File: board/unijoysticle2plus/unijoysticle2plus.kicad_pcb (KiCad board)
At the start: 2 copper layers, 62 x 49 mm, 47 parts, among them J1 DB9_Female, J2 DB9_Female, J3 USB_B_Micro, Q1 S8050, Q2 S8050, SW1 RESET, SW2 JOY SWAP, U1 74HC05, U2 74HC05, U3 74HC05, U4 ESP32-WROOM-32D, U5 AMS1117-3.3, U6 CP2102

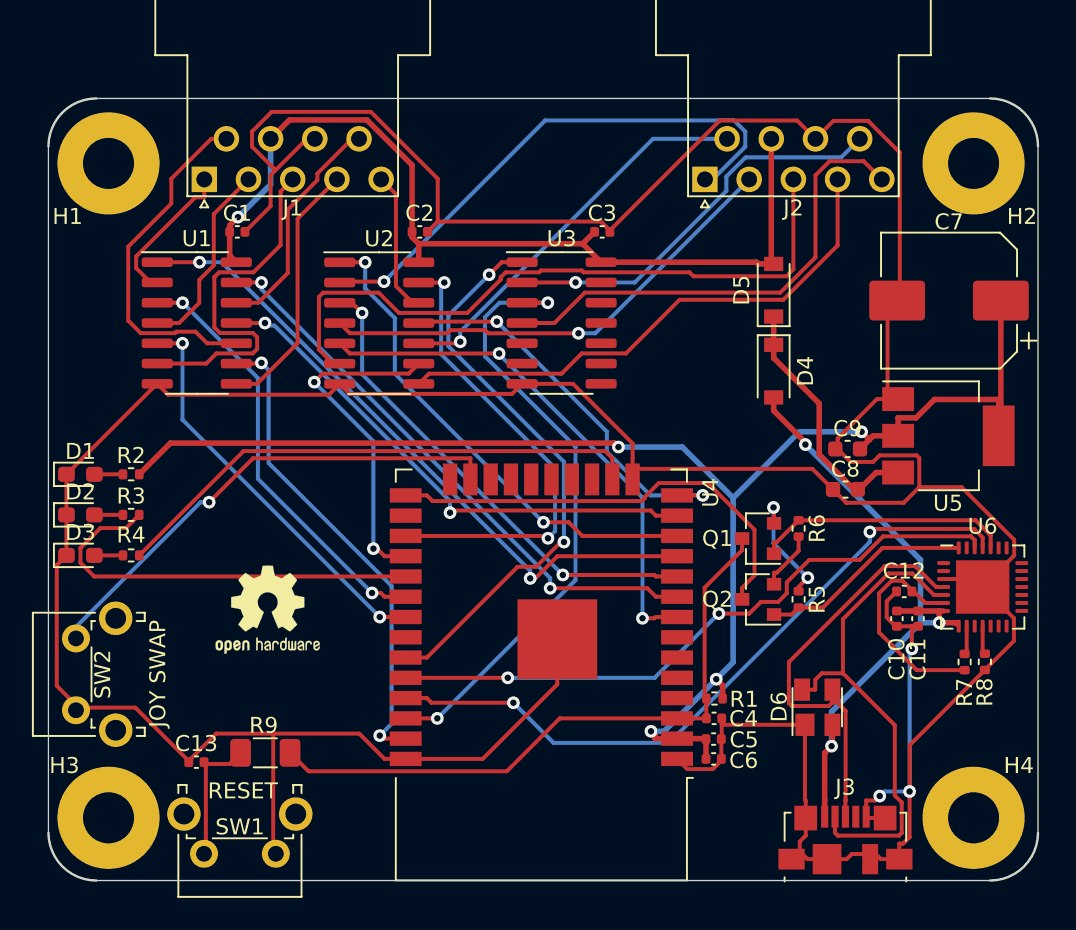
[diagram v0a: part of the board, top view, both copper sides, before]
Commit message: Unijoysticle2+ - Rev B: WIP
* 4 layer board
* hand-solder friendly
* Uses CH340C instead of CP2102
* Fixes placement of USB micro connector
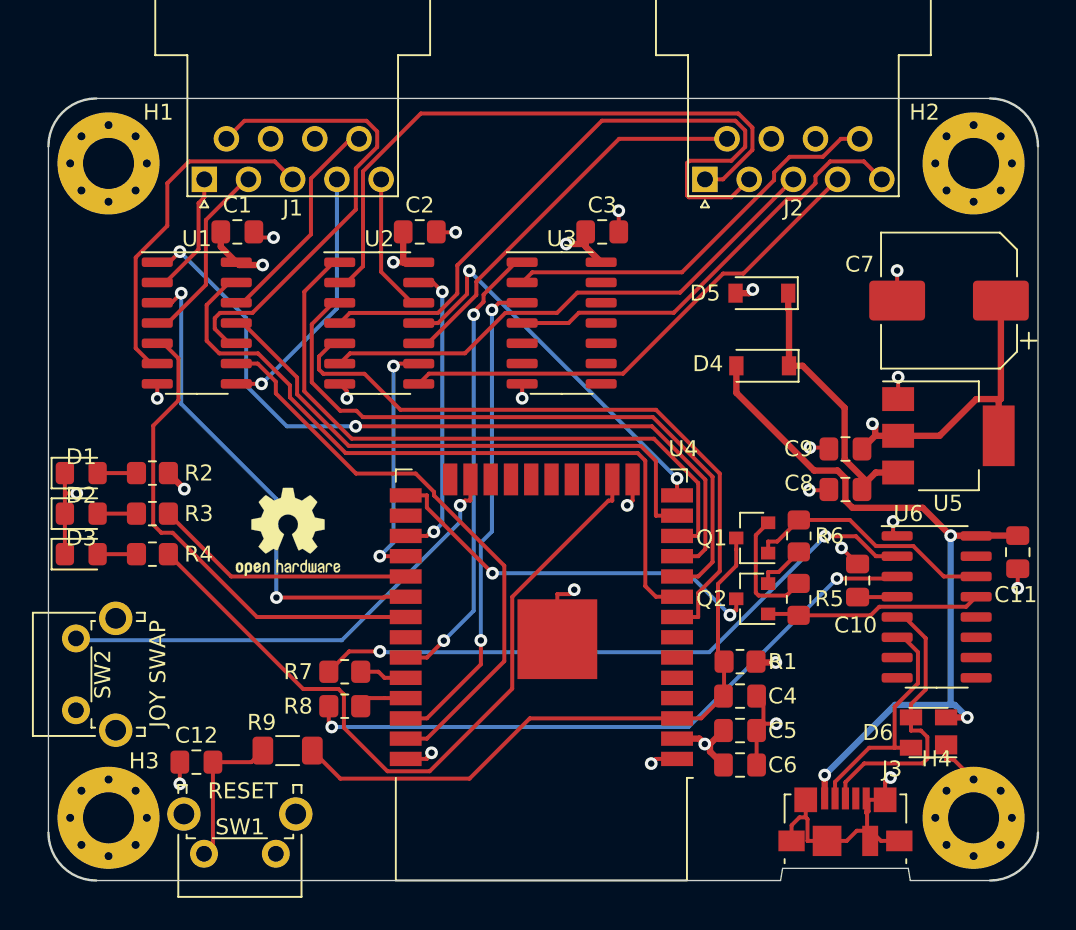
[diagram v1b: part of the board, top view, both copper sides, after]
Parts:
- removed the C12 at (93.9, 56.8)
- C1, C11, C2, C3, C4, C5, C6: footprint Capacitor_SMD:C_0402_1005Metric -> Capacitor_SMD:C_0805_2012Metric_Pad1.18x1.45mm_HandSolder
- C10: value 1uF -> .1uF; footprint Capacitor_SMD:C_0402_1005Metric -> Capacitor_SMD:C_0805_2012Metric_Pad1.18x1.45mm_HandSolder
- C12: renamed from C13; footprint Capacitor_SMD:C_0402_1005Metric -> Capacitor_SMD:C_0805_2012Metric_Pad1.18x1.45mm_HandSolder
- C8, C9: footprint Capacitor_SMD:C_0603_1608Metric -> Capacitor_SMD:C_0805_2012Metric_Pad1.18x1.45mm_HandSolder
- D1, D2, D3: footprint LED_SMD:LED_0603_1608Metric_Pad1.05x0.95mm_HandSolder -> LED_SMD:LED_0805_2012Metric_Pad1.15x1.40mm_HandSolder
- H1, H2, H3, H4: footprint MountingHole:MountingHole_3.2mm_M3_Pad -> MountingHole:MountingHole_3.2mm_M3_Pad_Via
- R1, R5, R6: footprint Resistor_SMD:R_0402_1005Metric -> Resistor_SMD:R_0805_2012Metric_Pad1.20x1.40mm_HandSolder
- R2, R3, R4: value 150 -> 330; footprint Resistor_SMD:R_0402_1005Metric -> Resistor_SMD:R_0805_2012Metric_Pad1.20x1.40mm_HandSolder
- R7: value 4.7k -> 1K; footprint Resistor_SMD:R_0402_1005Metric -> Resistor_SMD:R_0805_2012Metric_Pad1.20x1.40mm_HandSolder
- R8: value 10k -> 1K; footprint Resistor_SMD:R_0402_1005Metric -> Resistor_SMD:R_0805_2012Metric_Pad1.20x1.40mm_HandSolder
- U6: value CP2102 -> CH340C; footprint Package_DFN_QFN:QFN-28-1EP_5x5mm_P0.5mm_EP3.35x3.35mm -> Package_SO:SOIC-16_3.9x9.9mm_P1.27mm
- moved R8 40.2 mm to (58.8, 64.0), turned to 180 degrees
- moved R7 38.8 mm to (58.8, 61.8), turned to 180 degrees
- moved C11 7.51 mm to (101.0, 54.4)
- moved D6 7.15 mm to (95.4, 65.7), turned to 180 degrees
- moved REF** 5.04 mm to (55.2, 53.1)
- moved C10 3.43 mm to (90.9, 56.1), turned to 90 degrees
- moved U6 3.14 mm to (95.9, 57.8)
- moved R1 2.81 mm to (83.6, 61.2)
- moved C4 2.14 mm to (83.6, 63.4)
- moved C5 1.74 mm to (83.6, 65.5)
- moved C6 1.69 mm to (83.6, 67.7)
- moved R9 1.40 mm to (55.2, 66.8)
- moved R2 1.34 mm to (46.8, 49.4)
- moved R3 1.34 mm to (46.8, 51.9)
- moved R4 1.34 mm to (46.8, 54.5)
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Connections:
- C10 pad 1: VBUS -> Net-(C10-Pad1)
- H1 pad 1: (no net) -> GND
- H2 pad 1: (no net) -> GND
- H3 pad 1: (no net) -> GND
- H4 pad 1: (no net) -> GND
- R7 pad 1: Net-(C12-Pad1) -> /ESP_RXD
- R8 pad 1: Net-(R8-Pad1) -> /ESP_TXD
- R8 pad 2: GND -> Net-(R8-Pad2)
- U6 pad 1: (no net) -> GND
- U6 pad 11: Net-(R8-Pad1) -> (no net)
- U6 pad 13: (no net) -> /DTR_PROG
- U6 pad 14: (no net) -> /RTS_PROG
- U6 pad 16: (no net) -> VBUS
- U6 pad 2: (no net) -> Net-(R7-Pad2)
- U6 pad 3: GND -> Net-(R8-Pad2)
- U6 pad 4: /USBD+ -> Net-(C10-Pad1)
- U6 pad 5: /USBD- -> /USBD+
- U6 pad 6: Net-(C12-Pad1) -> /USBD-
- U6 pad 7: VBUS -> (no net)
- U6 pad 8: VBUS -> (no net)
- U6 pad 9: Net-(R7-Pad2) -> (no net)
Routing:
- net GND: track 296.1 -> 58.4 mm, vias 3 -> 21
- net +3V3: track 93.8 -> 27.0 mm
- net VDD: track 57.4 -> 12.2 mm, vias 1 -> 4
- net /ESP_TXD: track 44.1 -> 3.03 mm, vias 2 -> 0
- net Net-(R8-Pad2): track 0.00 -> 40.7 mm, vias 0 -> 2
- net Net-(R7-Pad2): track 1.79 -> 39.7 mm, vias 0 -> 2
- net /ESP_RXD: track 40.3 -> 2.98 mm, vias 2 -> 0
- net /USBD-: track 31.6 -> 15.0 mm
- net Net-(C12-Pad1): track 13.8 -> 0.00 mm
- net /J2_DOWN: track 30.1 -> 43.5 mm, vias 1 -> 0
- net /GPIO_J2_LED: track 33.9 -> 46.4 mm
- net /GPIO_J1_POTY: track 29.8 -> 18.8 mm
- net /GPIO_J2_DOWN: track 30.5 -> 41.5 mm, vias 2 -> 0
- net /GPIO_J1_LED: track 26.2 -> 16.5 mm
- net /GPIO_J2_UP: track 31.2 -> 40.9 mm, vias 2 -> 0
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- added copper zone on In1.Cu, net +3V3
- added copper zone on In2.Cu, net GND
- added copper zone on In1.Cu, net VDD
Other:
- outline, holes or cut-outs redrawn
- copper layers 2 -> 4
- net class POWER: trace_width 0.35 -> 0.4
- board text added: "Unijoysticle 2+ Rev. B"
- board text removed: "Unijoysticle 2+ Rev. A"

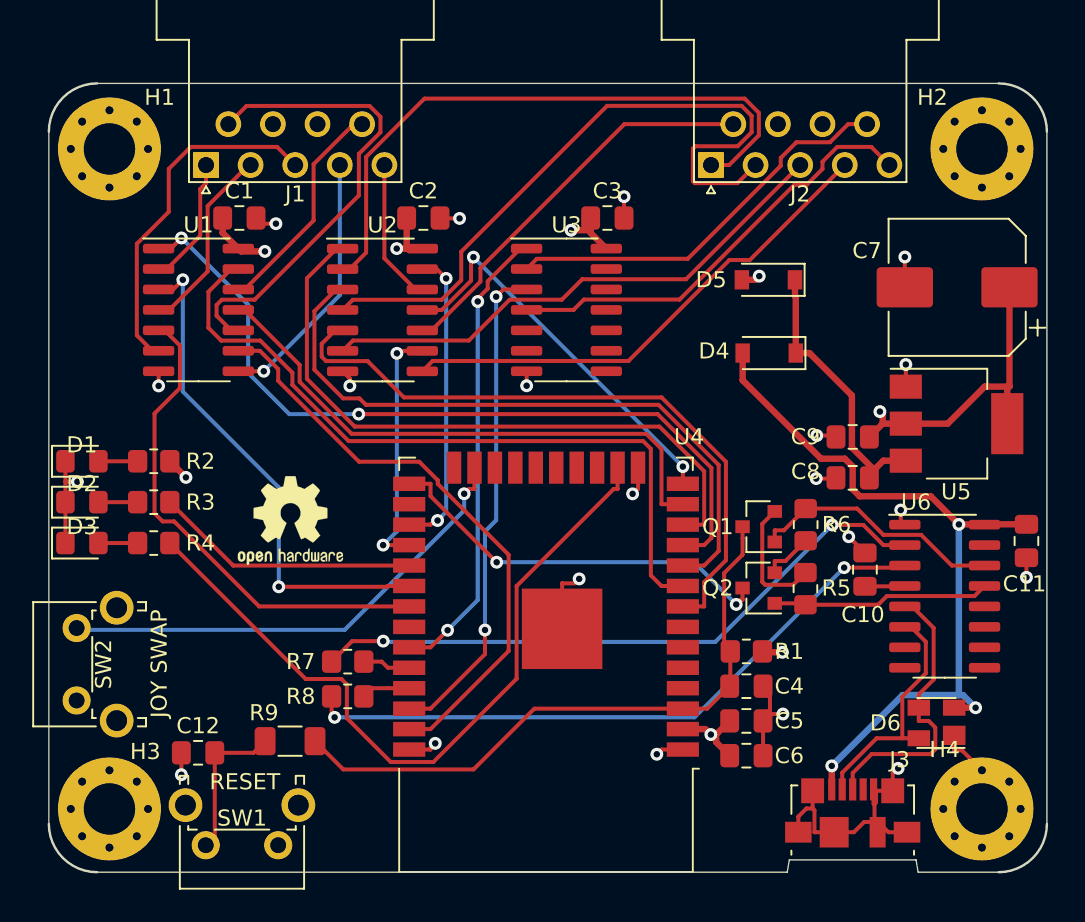
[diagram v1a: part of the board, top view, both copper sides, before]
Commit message: unijoysticle2+: rev b. JLCPCB fixes
Add LCSC reference to new components
Update LCSC reference of old components to use 0805
Power plane in layer is split in 3: VCC (C64 5+), 3v3+ and VBUS
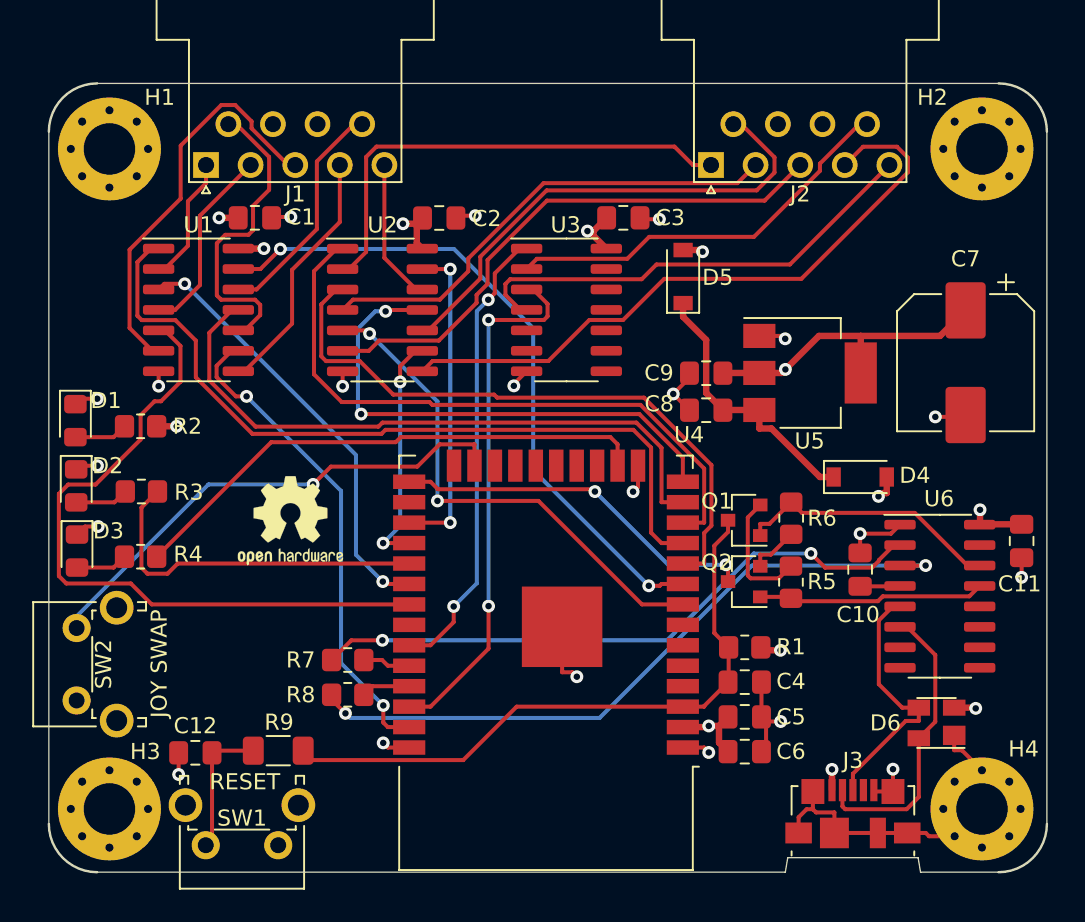
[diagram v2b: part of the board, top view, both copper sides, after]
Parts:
- D1: value LED POWER -> BLUE
- D2: value LED J1 -> GREEN
- D3: value LED J2 -> RED
- R2, R3, R4: value 330 -> 300
- moved C8 10.0 mm to (81.1, 46.2)
- moved C9 9.92 mm to (81.1, 43.9)
- moved U5 9.63 mm to (87.5, 43.9)
- moved D4 9.55 mm to (90.6, 50.4), turned to 0 degrees
- moved D5 5.30 mm to (79.6, 37.9), turned to 90 degrees
- moved C7 4.71 mm to (97.2, 43.3), turned to 270 degrees
- moved D1 2.56 mm to (41.9, 46.9), turned to 270 degrees
- moved R2 2.32 mm to (45.9, 47.2)
- moved R4 1.18 mm to (45.9, 55.3), turned to 0 degrees
- moved D2 1.07 mm to (41.9, 50.9), turned to 270 degrees
- moved R3 1.01 mm to (46.0, 51.3)
- moved C3 0.99 mm to (75.9, 34.3)
- moved C2 0.98 mm to (64.5, 34.3)
- moved Q1 0.98 mm to (83.4, 53.1)
- moved Q2 0.98 mm to (83.4, 56.9)
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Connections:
- R4 pad 1: /GPIO_J2_LED -> Net-(D3-Pad2)
- R4 pad 2: Net-(D3-Pad2) -> /GPIO_J2_LED
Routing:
- net VBUS: track 48.3 -> 7.76 mm, vias 3 -> 4
- net /J2_DOWN: track 43.5 -> 29.8 mm
- net /GPIO_J2_LED: track 46.4 -> 33.2 mm
- net /GPIO_J1_LEFT: track 31.0 -> 42.9 mm
- net /J1_FIRE: track 29.7 -> 19.5 mm
- net /GPIO_J2_LEFT: track 41.1 -> 31.8 mm, vias 0 -> 2
- net /J2_RIGHT: track 31.6 -> 40.9 mm
- net /J2_UP: track 39.2 -> 30.0 mm
- net /GPIO_J2_FIRE: track 24.8 -> 32.5 mm
- net /GPIO_J1_RIGHT: track 36.8 -> 30.3 mm, vias 0 -> 2
- net /J2_FIRE: track 25.1 -> 31.1 mm
- net /GPIO_J1_LED: track 16.5 -> 22.2 mm
- net /GPIO_J1_FIRE: track 35.2 -> 40.1 mm
- net /GPIO_J1_DOWN: track 31.4 -> 27.1 mm
- net /GPIO_J1_POTX: track 45.8 -> 42.0 mm, vias 0 -> 2
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- added copper zone on In1.Cu, net VBUS
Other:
- outline, holes or cut-outs redrawn

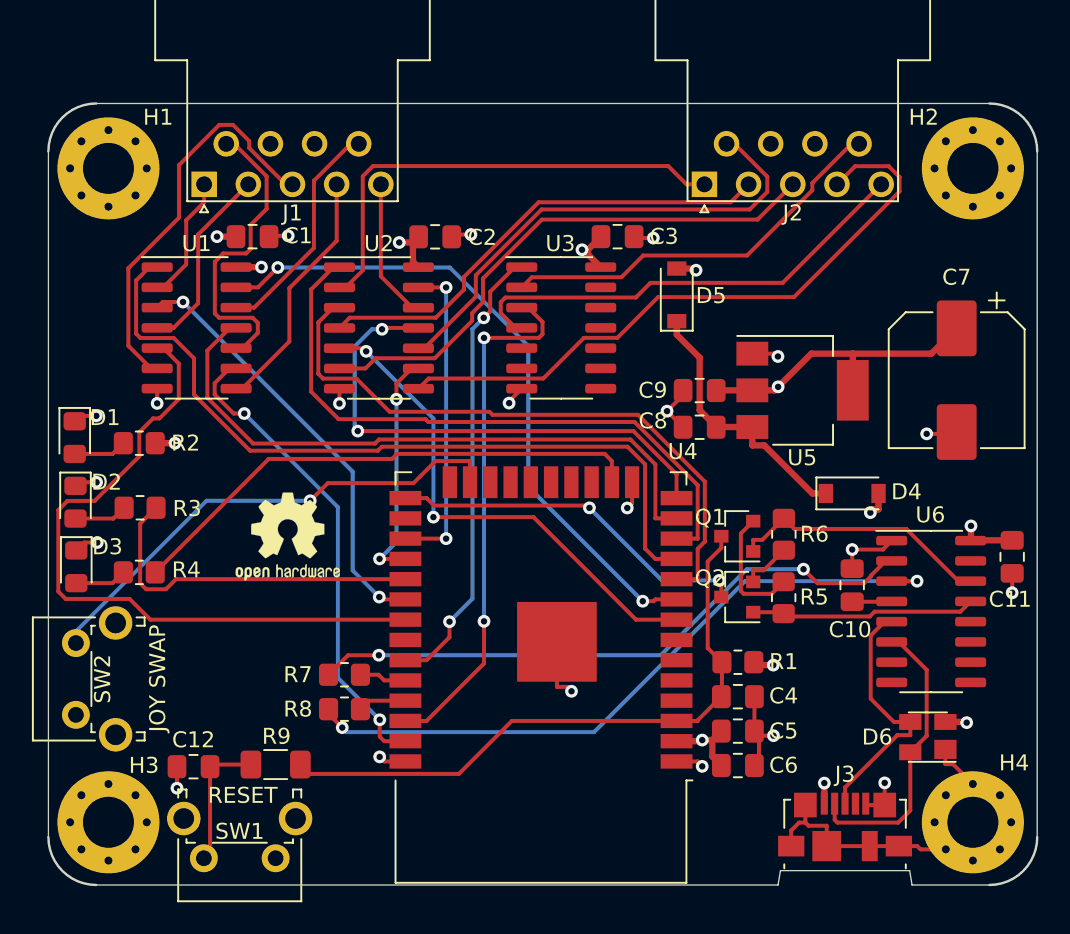
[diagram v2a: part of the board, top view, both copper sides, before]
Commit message: Unijoysticle2+: Rev C. WIP
Although I haven't tested yet Rev B., there a few changes that I wanted
to make to it.
Rev. C, so far, has the following changes:

- Switch Power plane with Ground place: Ground plane is #2 and Power
  plane #3.
- Manually routed: No longer uses auto-route. I think it is better for
  debugging to route it manually. More vias. Vias placed closer to the
  pads. Might reduce inductance (?).
- No longer using the ESD protector for USB. Almost nobody uses it,
  besides that CP2104 recommends it. But I'm no longer using CP2104, and
  CH340 doesn't mention it... I think it would be a good idea
  nonetheless, but only as an optional feature.
- Differential pair routing for USB D- and USB D+
- Mounting holes moved a tiny bit closer to the corners

Again, Rev. B might work perfectly well... waiting for it to arrive. But
I just wanted to make the above mentioned changes.
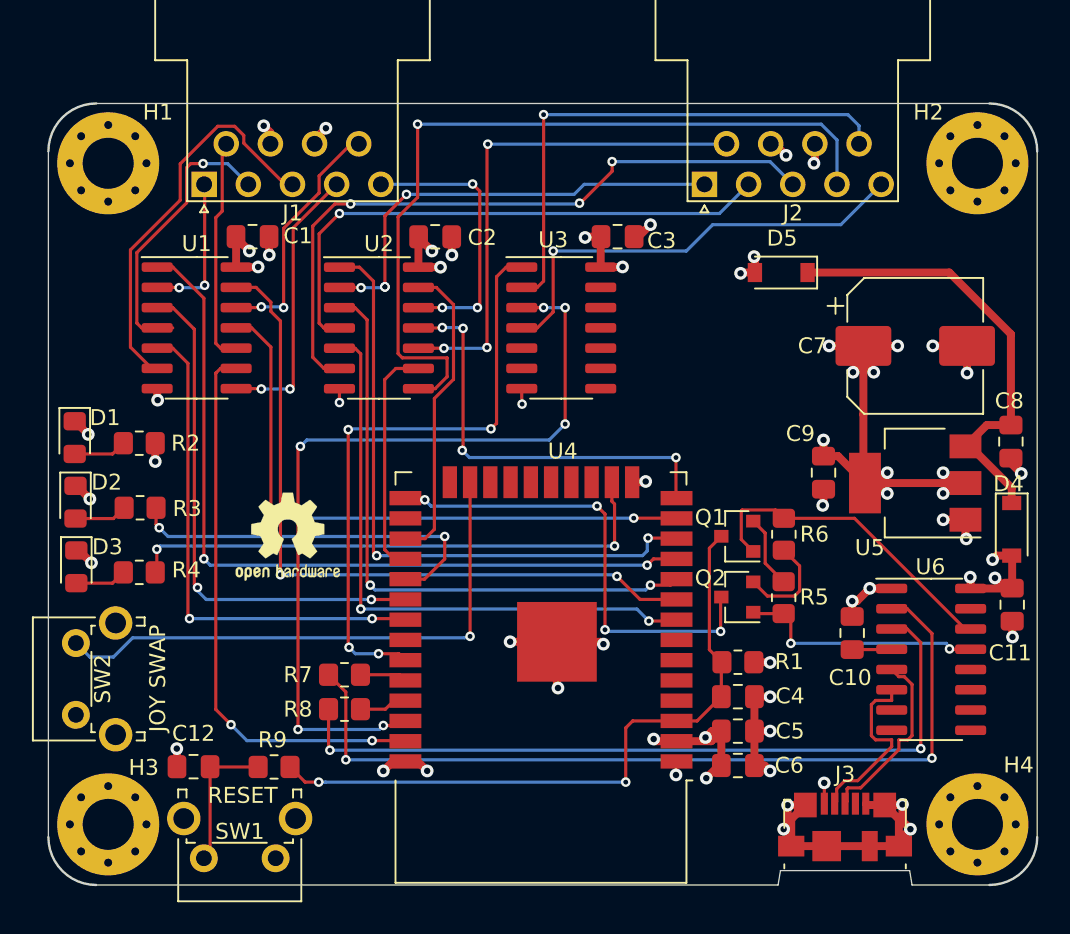
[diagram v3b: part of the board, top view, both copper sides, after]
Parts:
- removed D6: SP0503BAHT, Package_TO_SOT_SMD:SOT-143
- R9: footprint Resistor_SMD:R_1206_3216Metric_Pad1.30x1.75mm_HandSolder -> Resistor_SMD:R_0805_2012Metric_Pad1.20x1.40mm_HandSolder
- moved C8 19.5 mm to (100.6, 47.1), turned to 270 degrees
- moved D4 10.2 mm to (100.6, 52.6), turned to 270 degrees
- moved C9 9.32 mm to (88.8, 49.1), turned to 270 degrees
- moved U5 9.15 mm to (94.6, 49.7), turned to 180 degrees
- moved D5 6.70 mm to (86.2, 36.5), turned to 180 degrees
- moved C7 3.37 mm to (94.6, 41.1), turned to 0 degrees
- moved C10 3.00 mm to (90.6, 59.1)
- moved C11 3.00 mm to (100.7, 57.4)
- moved U6 3.00 mm to (95.6, 60.8)
- moved H2 0.43 mm to (98.5, 29.7)
- moved H1 0.32 mm to (44.0, 29.7)
- moved H4 0.31 mm to (98.5, 71.1)
- moved R9 0.18 mm to (54.4, 67.5)
- moved H3 0.13 mm to (44.0, 71.1)
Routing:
- net /GPIO_J2_POTY: track 33.0 -> 52.9 mm, vias 2 -> 6
- net +3V3: track 26.4 -> 43.6 mm, vias 4 -> 14
- net Net-(R7-Pad2): track 39.0 -> 53.6 mm
- net GND: track 58.2 -> 72.5 mm, vias 21 -> 35
- net Net-(C8-Pad1): track 16.9 -> 28.4 mm
- net /GPIO_J1_LEFT: track 42.9 -> 31.9 mm, vias 0 -> 2
- net /J2_RIGHT: track 40.9 -> 50.9 mm, vias 0 -> 1
- net /GPIO_J2_POTX: track 28.7 -> 38.0 mm, vias 2 -> 4
- net /J2_LEFT: track 34.4 -> 43.0 mm, vias 0 -> 3
- net /J1_POTY: track 8.94 -> 17.5 mm, vias 0 -> 3
- net VDD: track 10.0 -> 18.3 mm, vias 5 -> 10
- net /J2_POTX: track 25.1 -> 33.2 mm, vias 0 -> 1
- net /USBD-: track 18.3 -> 11.3 mm
- net /ESP_BOOT: track 22.9 -> 29.6 mm, vias 2 -> 4
- net /J1_DOWN: track 12.0 -> 17.9 mm, vias 0 -> 1
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- added copper zone on In2.Cu, net +3V3
- added copper zone on In1.Cu, net GND
- added copper zone on In2.Cu, net VBUS
- added copper zone on In2.Cu, net VDD
- removed copper zone on In1.Cu, net +3V3
- removed copper zone on In2.Cu, net GND
- removed copper zone on In1.Cu, net VBUS
- removed copper zone on In1.Cu, net VDD
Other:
- net class Default: trace_width 0.25 -> 0.2; via_dia 0.8 -> 0.6; via_drill 0.4 -> 0.3
- net class GND added: clearance 0.2, trace_width 0.5, via_dia 0.8, via_drill 0.4
- net class POWER: trace_width 0.4 -> 0.5
- board text added: "Unijoysticle 2+ Rev. C"
- board text removed: "Unijoysticle 2+ Rev. B"

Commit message: unijoysticle2plus: no idea
Unfortunately I have no idea what these changes are.
I would guess it is "safe" to commit them.
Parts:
- removed the H1 at (44.0, 29.7)
- removed the H2 at (98.5, 29.7)
- moved R5 0.45 mm to (86.8, 57.0)
- moved R6 0.44 mm to (86.8, 52.9), turned to 90 degrees
- renumbered H3 to H1, H4 to H2
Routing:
- net /DTR_PROG: track 15.5 -> 19.4 mm, vias 2 -> 0
- net Net-(Q1-Pad2): track 4.59 -> 8.16 mm
- net Net-(Q2-Pad2): track 6.37 -> 7.35 mm
- net /RTS_PROG: track 20.3 -> 21.3 mm
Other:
- outline, holes or cut-outs redrawn
